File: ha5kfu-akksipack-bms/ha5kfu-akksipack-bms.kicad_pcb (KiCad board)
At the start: 2 copper layers, 25.1 x 31.4 mm, 52 parts, among them IC1 BQ4050RSMR, J1 PACK, J2 PACK1, J3 PACK2, J4 COM, Q1 AON6512, Q2 AON6512, Q3 2N7002, Q4 AO3400A, Q5 AO3400A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

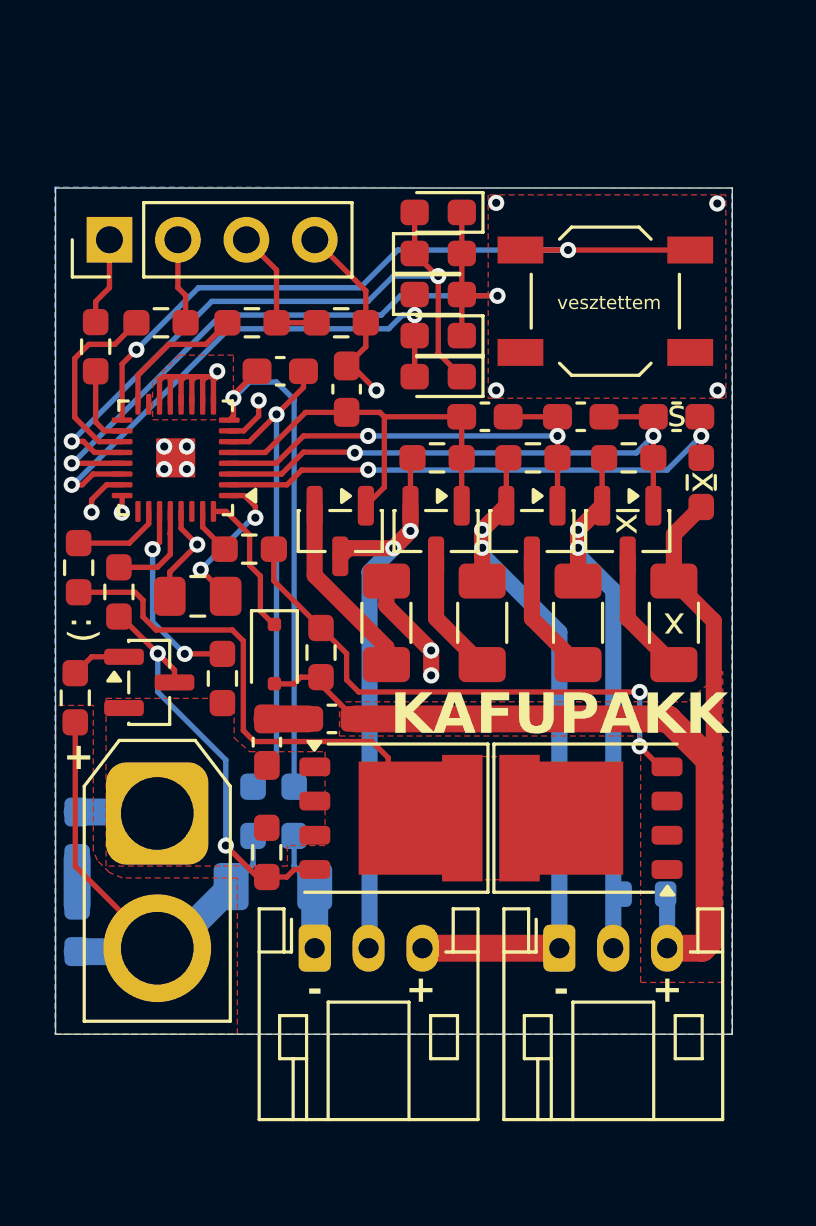
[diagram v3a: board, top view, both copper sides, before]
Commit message: Add mounting holes
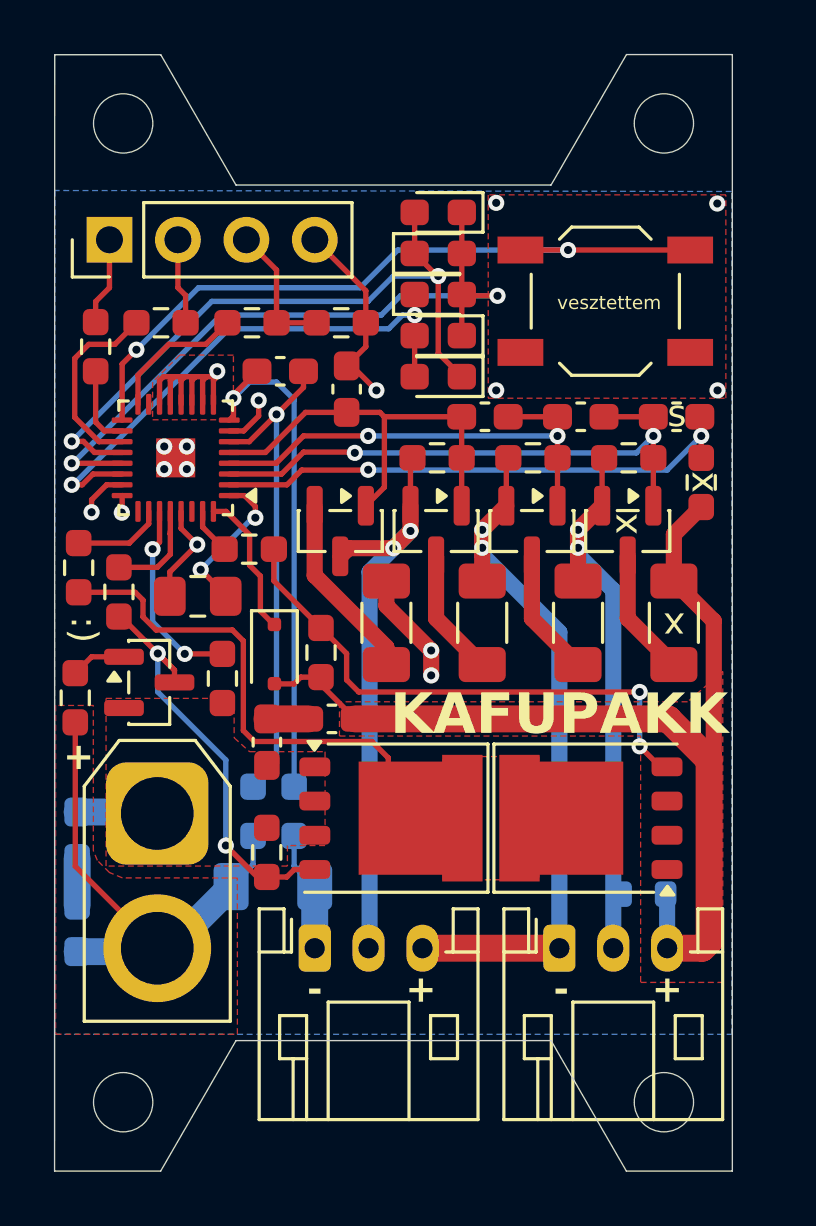
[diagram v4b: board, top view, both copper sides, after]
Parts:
- added REF**: MountingHole_2.2mm_M2, MountingHole:MountingHole_2.2mm_M2, F.Cu at (152.9, 92.2)
- added REF**: MountingHole_2.2mm_M2, MountingHole:MountingHole_2.2mm_M2, F.Cu at (173.0, 92.2)
- added REF**: MountingHole_2.2mm_M2, MountingHole:MountingHole_2.2mm_M2, F.Cu at (173.0, 128.5)
- added REF**: MountingHole_2.2mm_M2, MountingHole:MountingHole_2.2mm_M2, F.Cu at (152.9, 128.5)
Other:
- board size 25.1 x 31.4 mm -> 25.2 x 41.4 mm
